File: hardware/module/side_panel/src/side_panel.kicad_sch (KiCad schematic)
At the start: 47 parts, among them J1 Top Connector, J3 Conn_01x05, J5 Conn_02x07_Odd_Even, M1 GA12-N20 12V 60rpm, Q1 AP2302B, U1 PY32F003F1xPx, U2 L9110S, U3 ITR8307, U4 ITR8307, U5 ITR8307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

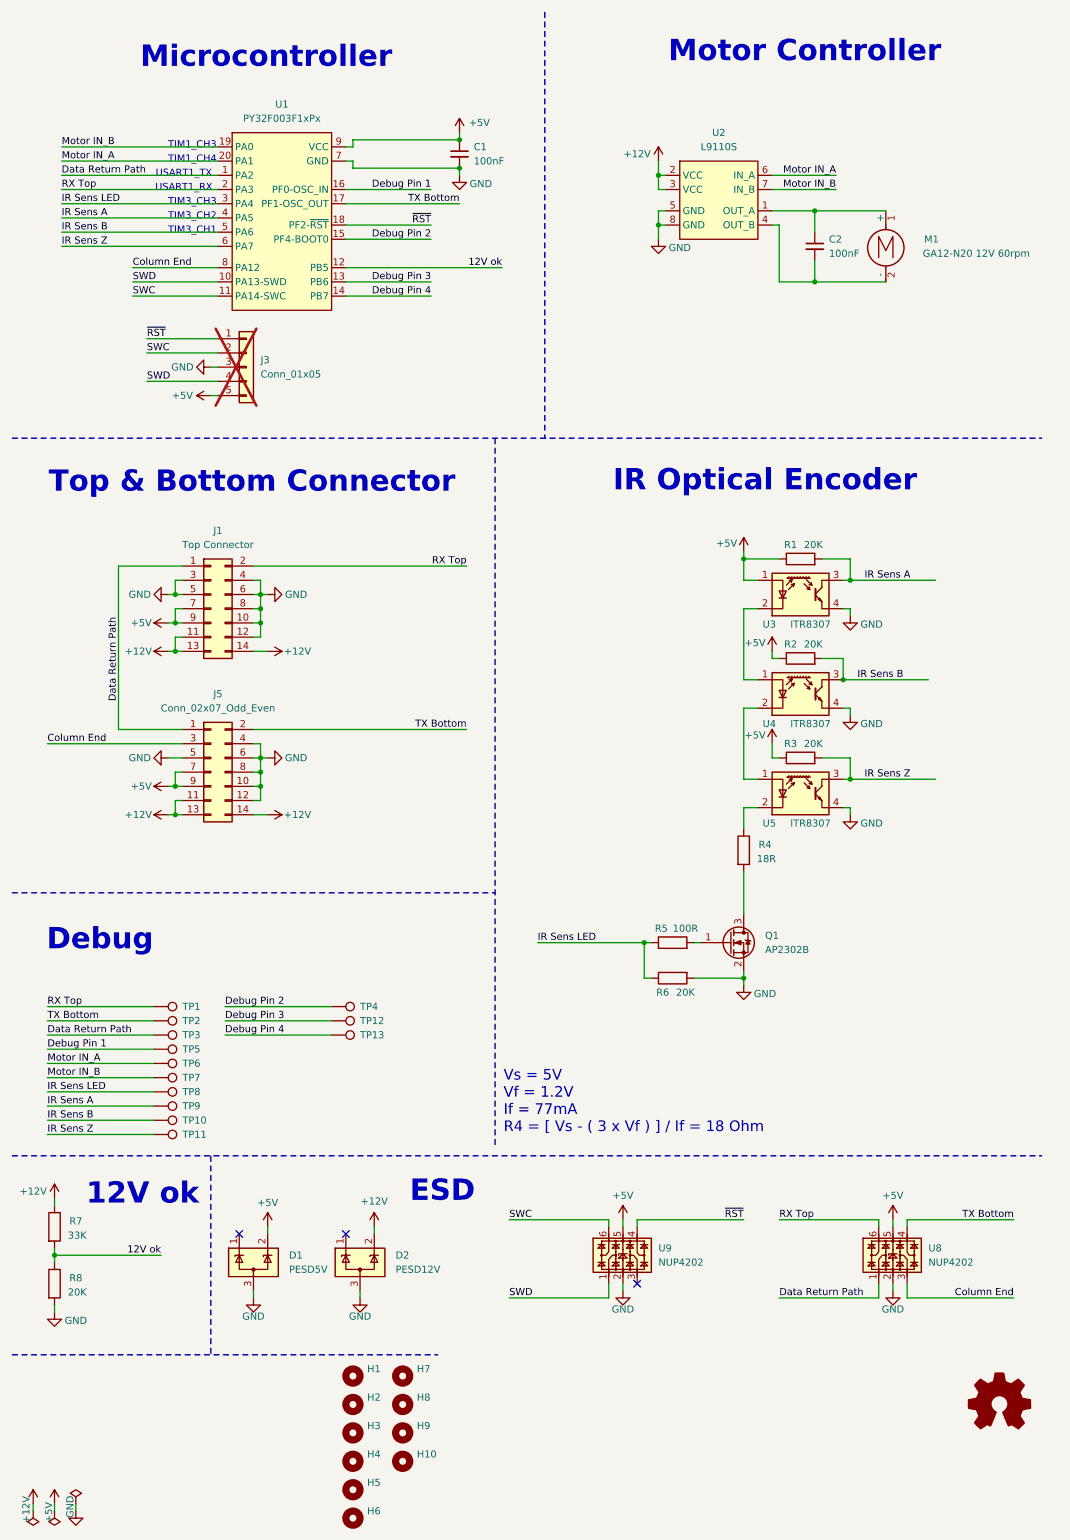
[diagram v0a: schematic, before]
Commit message: rework sidepanel to 3 sensors, ad 12V ok signal, add debug uart, change test points for skedd connector
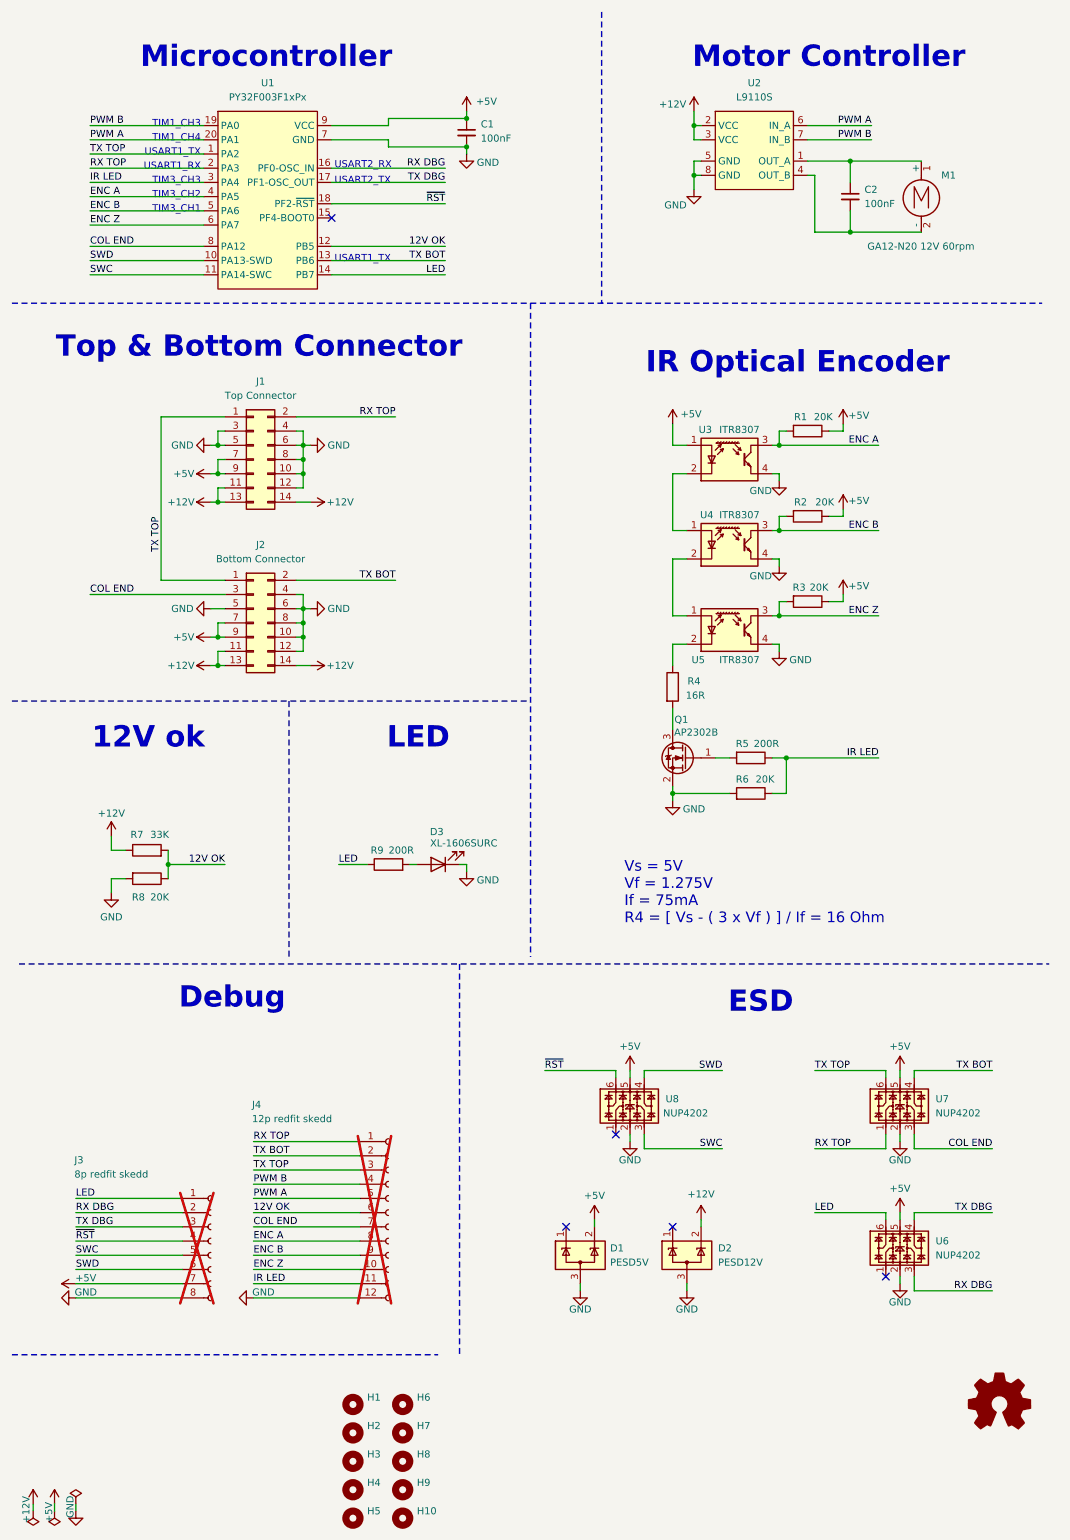
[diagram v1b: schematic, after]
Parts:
- removed J3: Conn_01x05, Connector_PinHeader_2.54mm:PinHeader_1x05_P2.54mm_Vertical, symbol Connector_Generic:Conn_01x05
- removed TP1, TP10, TP11, TP12, TP13, TP2, TP3, TP4, TP5, TP6, TP7, TP8, TP9: TestPoint, TestPoint:TestPoint_THTPad_D2.5mm_Drill1.2mm, symbol Connector:TestPoint
- added D3: XL-1606SURC, LED_SMD:LED_Kingbright_APA1606_1.6x0.6mm_Horizontal, symbol Device:LED
- added J3: 8p redfit skedd, Skedd Connector:490107670812, symbol Connector:Conn_01x08_Socket
- added J4: 12p redfit skedd, Skedd Connector:490107671212, symbol Connector:Conn_01x12_Socket
- added R9: 200R, Resistor_SMD:R_0805_2012Metric, symbol Device:R
- added U6: NUP4202, Package_TO_SOT_SMD:SOT-23-6, symbol Power_Protection:NUP4202
- J2: renamed from J5; value Conn_02x07_Odd_Even -> Bottom Connector
- R4: value 18R -> 16R
- R5: value 100R -> 200R
- renumbered U8 to U7, U9 to U8
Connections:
- net +5V: now also J3.7 (Pin_7), U6.5
- net GND: now also D3.1 (K), J3.8 (Pin_8), J4.12 (Pin_12), U6.2
- net SWC: now also U8.3, J3.5 (Pin_5); no longer U8.6
- net SWD: now also U8.4, J3.6 (Pin_6); no longer U8.1
- net ~{RST}: now also U8.6, J3.4 (Pin_4); no longer U8.4
- net 12V ok renamed 12V OK
- net 12V OK: now also J4.6 (Pin_6)
- net Column End renamed COL END
- net COL END: now also J4.7 (Pin_7)
- net Data Return Path renamed TX TOP
- net TX TOP: now also U7.6, J4.3 (Pin_3); no longer U7.1
- net Debug Pin 1 renamed RX DBG
- net RX DBG: now also J3.2 (Pin_2), U6.3
- net Debug Pin 2: no longer names the net of U1.15 (PF4-BOOT0)
- net Debug Pin 3 renamed TX BOT
- net TX BOT: now also J2.2 (Pin_2), U7.4, J4.2 (Pin_2)
- net Debug Pin 4 renamed LED
- net LED: now also J3.1 (Pin_1), R9.1, U6.6
- net IR Sens A renamed ENC A
- net ENC A: now also J4.8 (Pin_8)
- net IR Sens B renamed ENC B
- net ENC B: now also J4.9 (Pin_9)
- net IR Sens LED renamed IR LED
- net IR LED: now also J4.11 (Pin_11)
- net IR Sens Z renamed ENC Z
- net ENC Z: now also J4.10 (Pin_10)
- net Motor IN_A renamed PWM A
- net PWM A: now also J4.5 (Pin_5)
- net Motor IN_B renamed PWM B
- net PWM B: now also J4.4 (Pin_4)
- net RX Top renamed RX TOP
- net RX TOP: now also U7.1, J4.1 (Pin_1); no longer U7.6
- removed net TX Bottom: J2.2 (Pin_2), U1.17 (PF1-OSC_OUT), U7.4
- new net: D3.2 (A), R9.2
- new net TX DBG: J3.3 (Pin_3), U1.17 (PF1-OSC_OUT), U6.4
- no-connect marks 3 -> 5
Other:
- note added: "LED"
- note added: "USART2_RX"
- note added: "USART2_TX"
- note added: "Vs = 5V Vf = 1.275V If = 75mA R4 = [ Vs - ( 3 x Vf ) ] / If = 16 Ohm"
- note removed: "Vs = 5V Vf = 1.2V If = 77mA R4 = [ Vs - ( 3 x Vf ) ] / If = 18 Ohm"
- moved on the sheet: C1, C2, D1, D2, H1, H10, H2, H3, H4, H5, H6, H7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

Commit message: Add onboard 3.3V regulator to side panal so that uart communication may switch to 3.3V
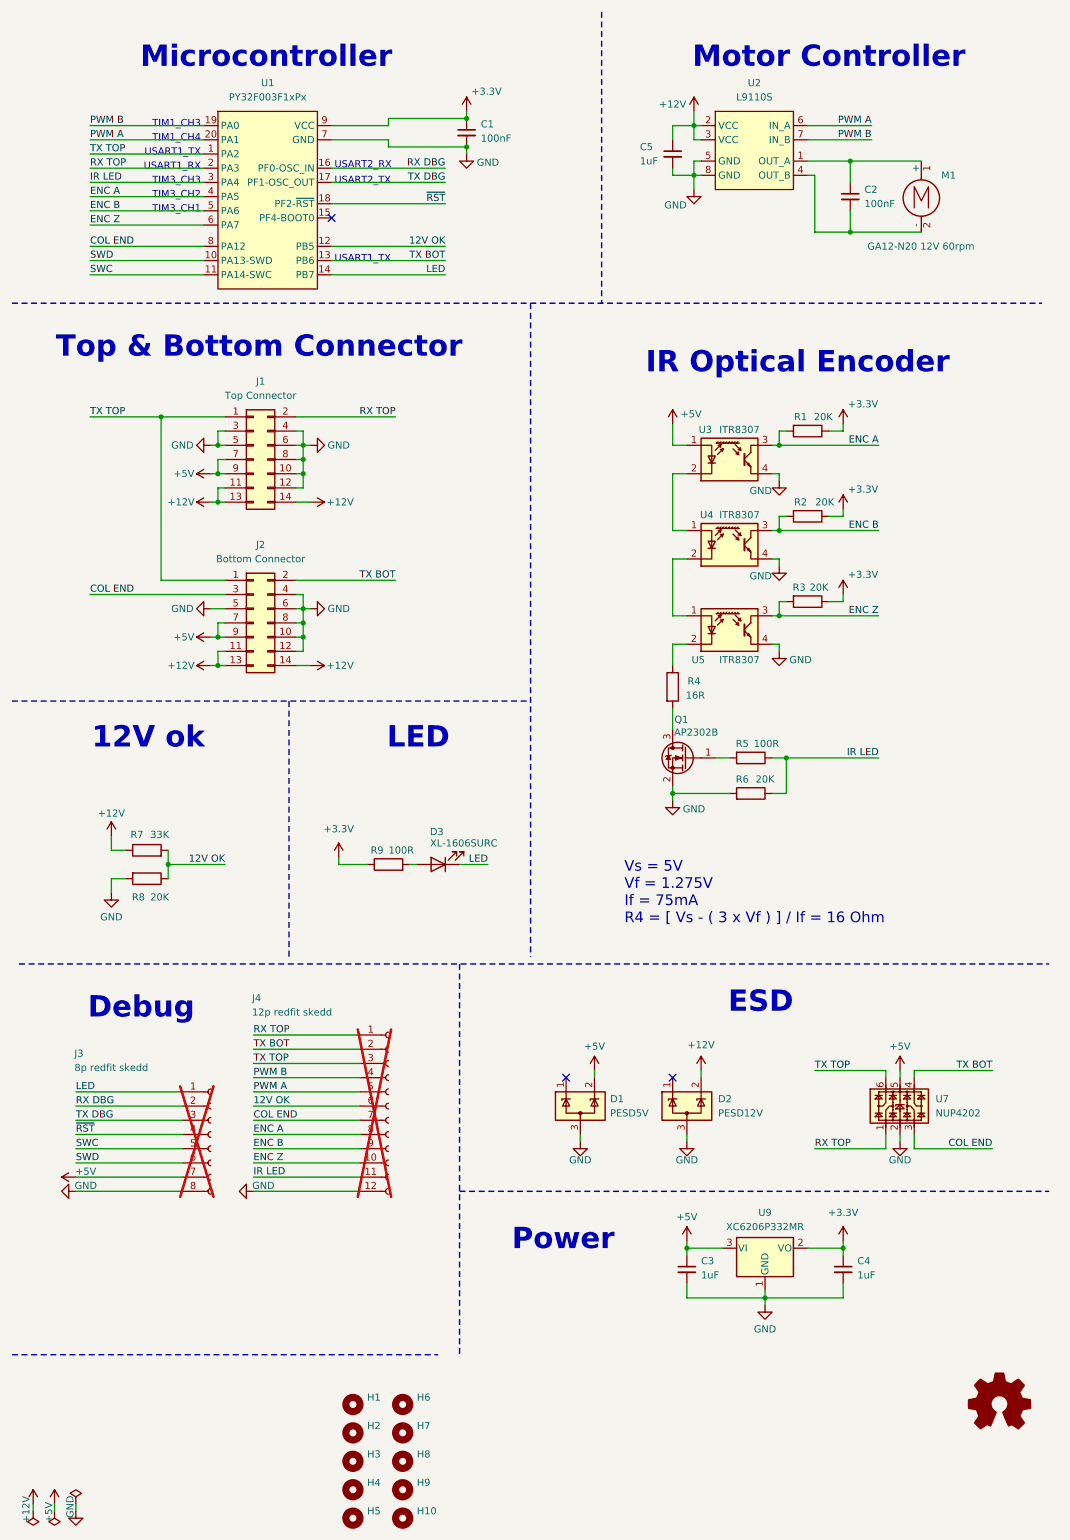
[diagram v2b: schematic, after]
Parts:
- removed U6, U8: NUP4202, Package_TO_SOT_SMD:SOT-23-6, symbol Power_Protection:NUP4202
- added C3, C4, C5: 1uF, Capacitor_SMD:C_0805_2012Metric, symbol Device:C_Small
- added U9: XC6206P332MR, Package_TO_SOT_SMD:SOT-23-3, symbol Regulator_Linear:XC6206PxxxMR
- R5, R9: value 200R -> 100R
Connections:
- net +12V: now also C5.1
- net +5V: now also C3.1, U9.3 (VI); no longer C1.1, R1.1, R2.1, R3.1, U1.9 (VCC)
- net GND: now also C3.2, C4.2, C5.2, U9.1 (GND); no longer D3.1 (K)
- net LED: now also D3.1 (K); no longer R9.1
- new net +3.3V: C1.1, C4.1, R1.1, R2.1, R3.1, R9.1, U1.9 (VCC), U9.2 (VO)
- no-connect marks 5 -> 3
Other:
- note added: "Power"
- moved on the sheet: D1, D2, J3, J4

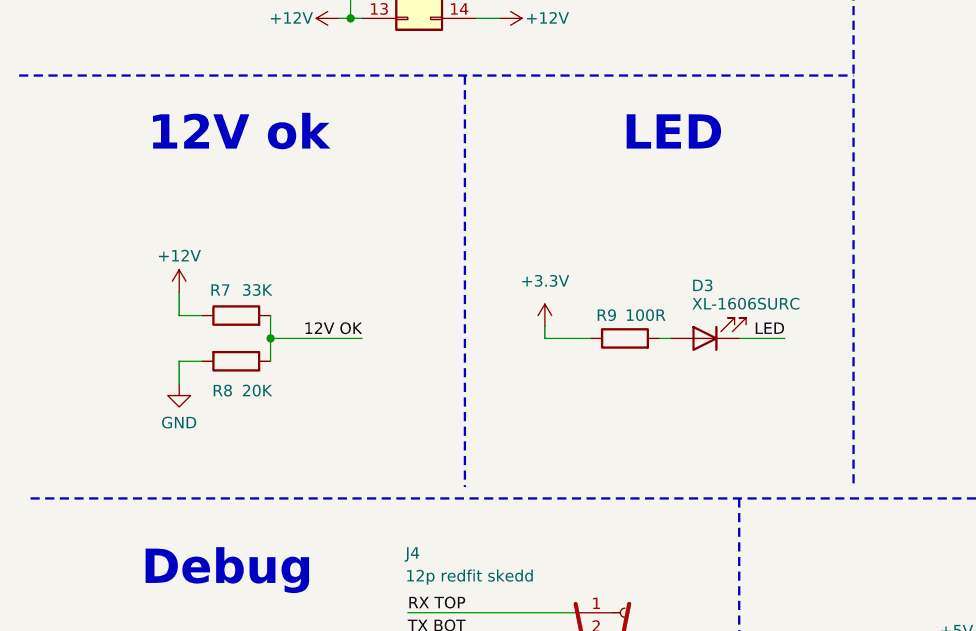
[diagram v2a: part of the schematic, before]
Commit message: Optimize flap latch shape.
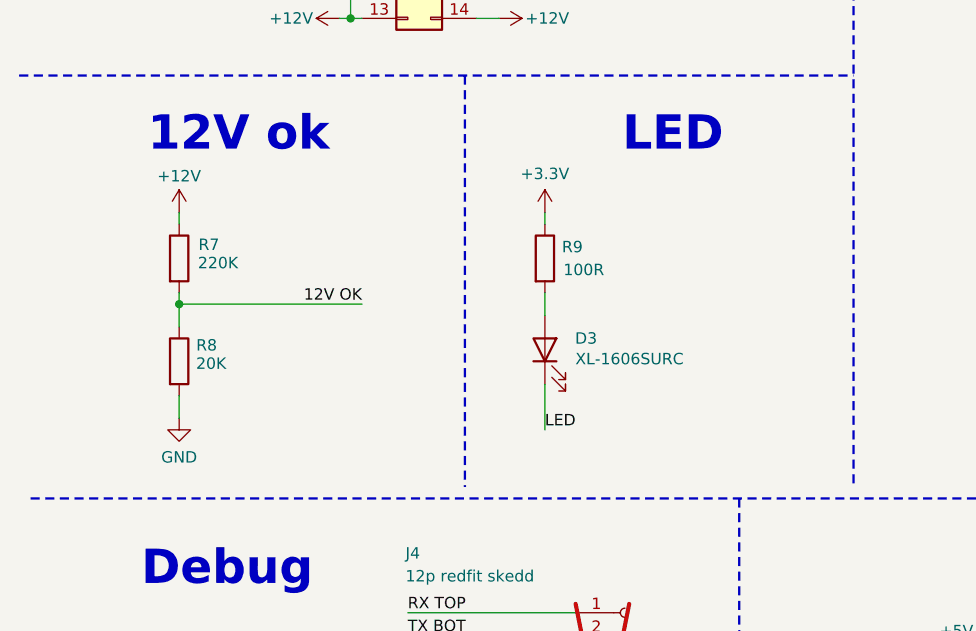
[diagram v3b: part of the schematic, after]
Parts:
- R7: value 33K -> 220K
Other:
- moved on the sheet: D3, R7, R8, R9

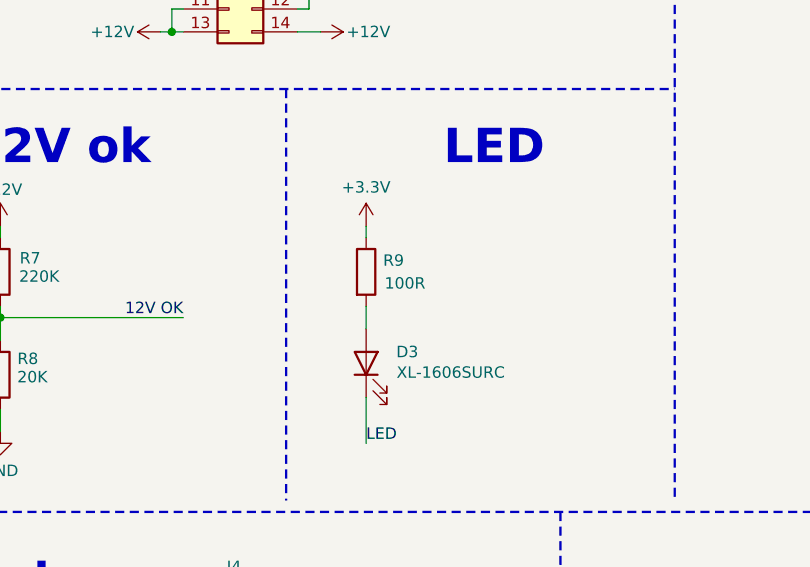
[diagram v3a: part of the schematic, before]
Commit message: fix erroneous U4 angle from 45 to 37.5
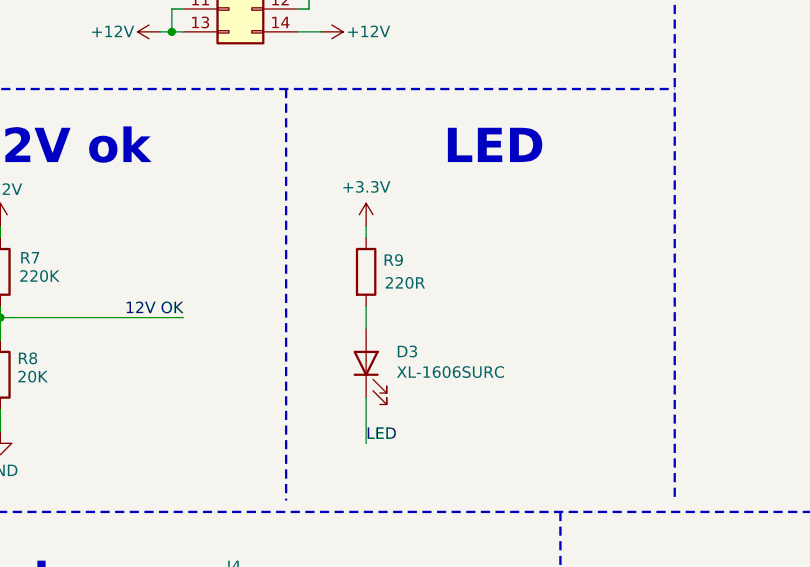
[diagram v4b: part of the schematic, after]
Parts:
- R9: value 100R -> 220R
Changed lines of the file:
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@@
 		(title "Side Panel")
 		(date "${DATE}")
-		(rev "7.2.0")
+		(rev "7.3.0")
 		(company "OpenFlap")
 		(comment 1 "${GIT_TAG}")
@@
 			)
 		)
-		(property "Value" "100R"
+		(property "Value" "220R"
 			(at 75.438 157.48 0)
 			(effects

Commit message: Bugfixes and testing, working module & controller
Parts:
- R7: value 220K -> 75K
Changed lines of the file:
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@@
 		(title "Side Panel")
 		(date "${DATE}")
-		(rev "7.3.0")
+		(rev "7.3.1")
 		(company "OpenFlap")
 		(comment 1 "${GIT_TAG}")
@@
 			)
 		)
-		(property "Value" "220K"
+		(property "Value" "75K"
 			(at 34.798 156.718 0)
 			(effects

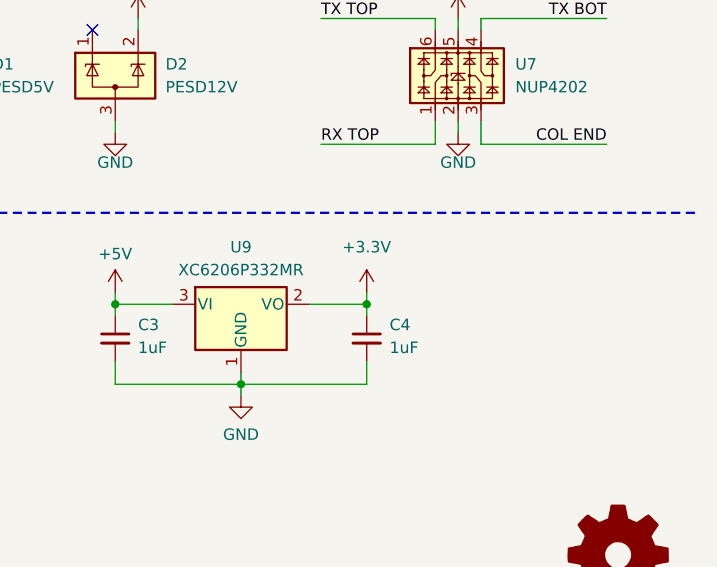
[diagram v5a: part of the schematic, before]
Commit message: Add test points to pcb's
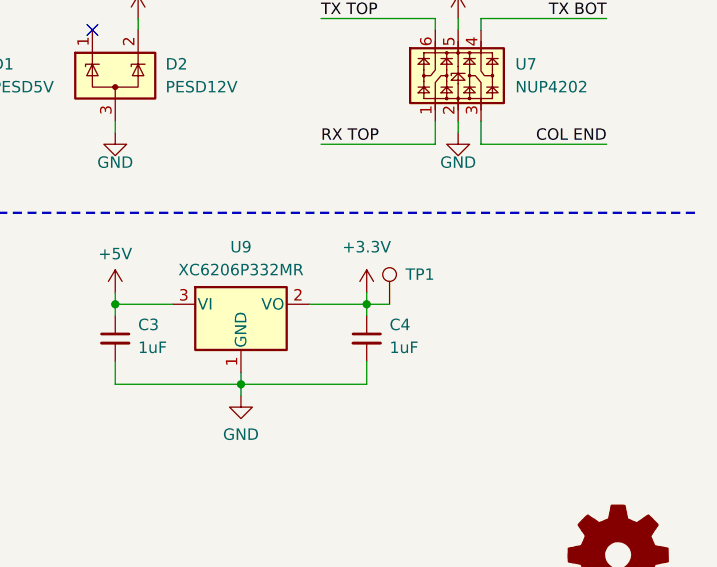
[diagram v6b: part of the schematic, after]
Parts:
- added TP1: TestPoint, TestPoint:TestPoint_Pad_D1.5mm, symbol Connector:TestPoint
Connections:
- net +3.3V: now also TP1.1
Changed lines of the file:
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@@
 		(title "Side Panel")
 		(date "${DATE}")
-		(rev "7.3.1")
+		(rev "7.3.2")
 		(company "OpenFlap")
 		(comment 1 "${GIT_TAG}")
@@
 	(wire
 		(pts
+			(xy 161.29 233.68) (xy 163.83 233.68)
+		)
+		(stroke
+			(width 0)
+			(type default)
+		)
+	)
+	(wire
+		(pts
 			(xy 26.67 45.72) (xy 46.99 45.72)
 		)
@@
 					(unit 1)
 				)
+			)
+		)
+	)
+	(symbol
+		(lib_id "Connector:TestPoint")
+		(at 163.83 233.68 0)
+		(unit 1)
+		(exclude_from_sim no)
+		(in_bom yes)
+		(on_board yes)
+		(dnp no)
+		(property "Reference" "TP1"
+			(at 165.608 230.378 0)
+			(effects
+				(font
+					(size 1.27 1.27)
+				)
+				(justify left)
+			)
+		)
+		(property "Value" "TestPoint"
+			(at 165.1 228.6 90)
+			(effects
+				(font
+					(size 1.27 1.27)
+				)
+				(justify left)
+				(hide yes)
+			)
+		)
+		(property "Footprint" "TestPoint:TestPoint_Pad_D1.5mm"
+			(at 168.91 233.68 0)
+			(effects
+				(font
+					(size 1.27 1.27)
+				)
+				(hide yes)
+			)
+		)
+		(property "Datasheet" "~"
+			(at 168.91 233.68 0)
+			(effects
+				(font
+					(size 1.27 1.27)
+				)
+				(hide yes)
+			)
+		)
+		(property "Description" "test point"
+			(at 163.83 233.68 0)
+			(effects
+				(font
+					(size 1.27 1.27)
+				)
+				(hide yes)
+			)
+		)
+		(pin "1"
+		)
+		(instances
+			(project "side_panel"
+				(path "/36bb1b3b-7b5b-4a4c-b4db-cfb27ceb38a1"
+					(reference "TP1")
+					(unit 1)
+				)
